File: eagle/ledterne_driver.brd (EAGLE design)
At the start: 25.9 x 24.6 mm, 15 parts, among them IC1 MEGA8-AI

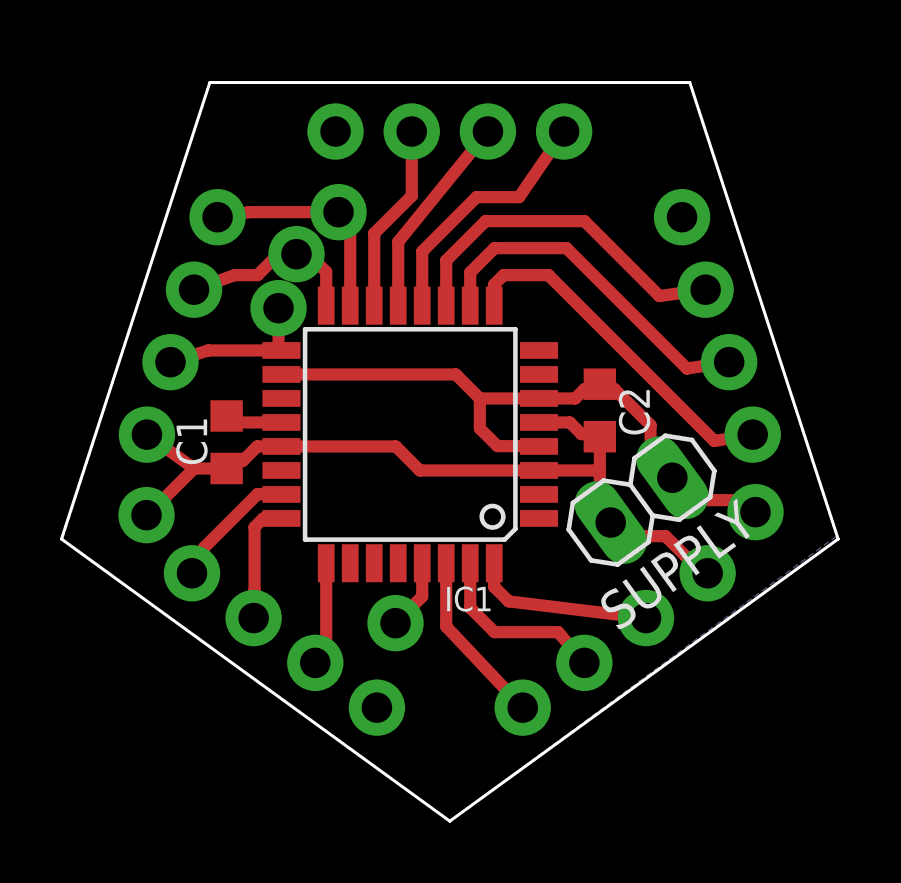
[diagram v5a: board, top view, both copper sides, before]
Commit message: Switch to a slightly larger capacitor package
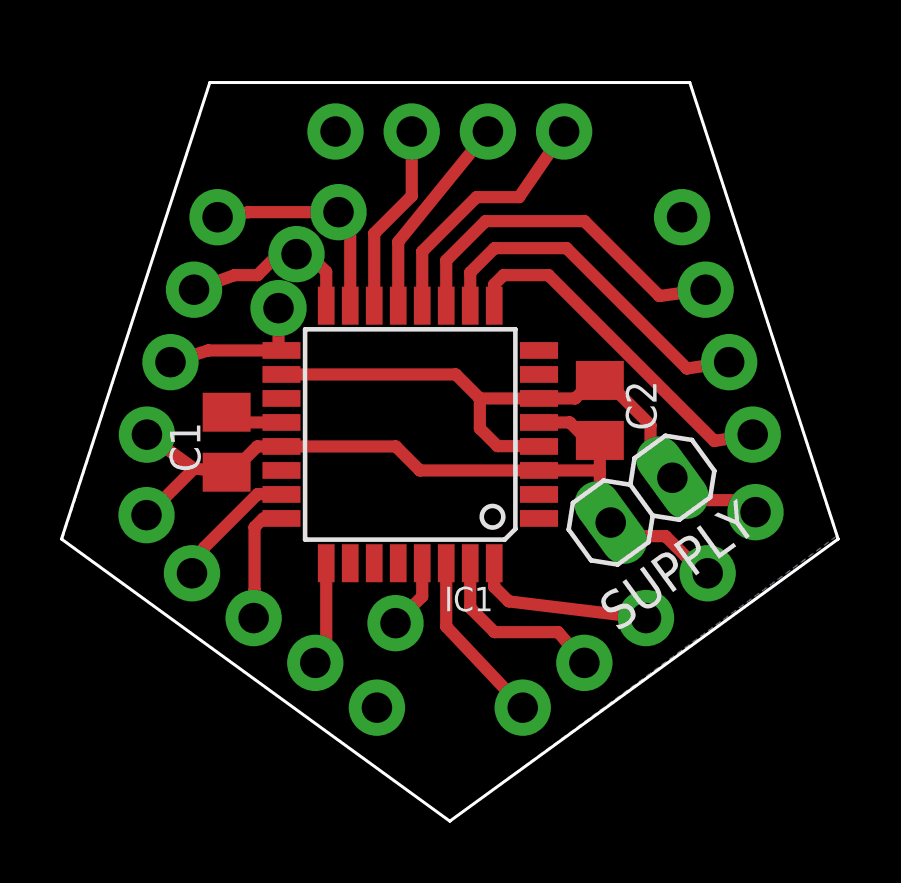
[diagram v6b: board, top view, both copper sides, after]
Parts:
- C1, C2: device rcl:C0603K -> rcl:C0805K
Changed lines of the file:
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@@
 <attribute name="MPN" value="ATMEGA8-16AU" x="15.19" y="15.79" size="1.778" layer="27" rot="R180" display="off"/>
 </element>
-<element name="C1" library="rcl" package="C0603K" value="100n" x="9.07" y="15.53" rot="R90"/>
-<element name="C2" library="rcl" package="C0603K" value="100n" x="21.51" y="16.59" rot="R270"/>
+<element name="C1" library="rcl" package="C0805K" value="100n" x="9.07" y="15.53" rot="R90"/>
+<element name="C2" library="rcl" package="C0805K" value="100n" x="21.51" y="16.59" rot="R270"/>
 <element name="JP1" library="pinhead_round_pads" package="1X04/90" value="" x="16.51" y="29.69815625" rot="MR0"/>
 <element name="JP2" library="pinhead_round_pads" package="1X04/90" value="" x="29.05268125" y="20.5853625" rot="MR72"/>
@@
 <wire x1="15.51" y1="14.59" x2="14.71" y2="15.39" width="0.4064" layer="1"/>
 <wire x1="14.71" y1="15.39" x2="10.8974" y2="15.39" width="0.4064" layer="1"/>
-<wire x1="21.51" y1="15.715" x2="21.51" y2="14.5" width="0.4064" layer="1"/>
+<wire x1="21.51" y1="15.59" x2="21.51" y2="14.5" width="0.4064" layer="1"/>
 <wire x1="21.51" y1="14.5" x2="21.51" y2="13.216059375" width="0.4064" layer="1"/>
 <wire x1="21.51" y1="13.216059375" x2="21.872546875" y2="12.8535125" width="0.4064" layer="1"/>
 <wire x1="19.4826" y1="14.59" x2="21.42" y2="14.59" width="0.4064" layer="1"/>
 <wire x1="21.42" y1="14.59" x2="21.51" y2="14.5" width="0.4064" layer="1"/>
-<wire x1="9.07" y1="14.655" x2="7.984796875" y2="14.655" width="0.4064" layer="1"/>
+<wire x1="9.07" y1="14.53" x2="7.984796875" y2="14.655" width="0.4064" layer="1"/>
 <wire x1="7.984796875" y1="14.655" x2="6.413490625" y2="15.78448125" width="0.4064" layer="1"/>
 <wire x1="19.4826" y1="16.19" x2="20.51" y2="16.19" width="0.4064" layer="1"/>
 <wire x1="20.51" y1="16.19" x2="20.9" y2="15.8" width="0.4064" layer="1"/>
 <wire x1="20.9" y1="15.8" x2="21.425" y2="15.8" width="0.4064" layer="1"/>
-<wire x1="21.425" y1="15.8" x2="21.51" y2="15.715" width="0.4064" layer="1"/>
+<wire x1="21.425" y1="15.8" x2="21.51" y2="15.59" width="0.4064" layer="1"/>
 <wire x1="21.872546875" y1="12.8535125" x2="22.326059375" y2="12.4" width="0.4064" layer="1"/>
 <wire x1="22.326059375" y1="12.4" x2="23.7" y2="12.4" width="0.4064" layer="1"/>
@@
 <wire x1="10.09" y1="15.39" x2="9.6" y2="14.9" width="0.4064" layer="1"/>
 <wire x1="9.6" y1="14.9" x2="9.315" y2="14.9" width="0.4064" layer="1"/>
-<wire x1="9.315" y1="14.9" x2="9.07" y2="14.655" width="0.4064" layer="1"/>
+<wire x1="9.315" y1="14.9" x2="9.07" y2="14.53" width="0.4064" layer="1"/>
 <wire x1="6.4" y1="13.1" x2="6.429796875" y2="13.1" width="0.4064" layer="1"/>
 <wire x1="6.429796875" y1="13.1" x2="7.984796875" y2="14.655" width="0.4064" layer="1"/>
@@
 <wire x1="20.69" y1="16.99" x2="21" y2="17.3" width="0.4064" layer="1"/>
 <wire x1="21" y1="17.3" x2="21.345" y2="17.3" width="0.4064" layer="1"/>
-<wire x1="21.345" y1="17.3" x2="21.51" y2="17.465" width="0.4064" layer="1"/>
+<wire x1="21.345" y1="17.3" x2="21.51" y2="17.59" width="0.4064" layer="1"/>
 <wire x1="21.345" y1="17.3" x2="22" y2="17.3" width="0.4064" layer="1"/>
 <wire x1="22" y1="17.3" x2="23.2" y2="16.1" width="0.4064" layer="1"/>
@@
 <contactref element="IC1" pad="20"/>
 <wire x1="10.8974" y1="16.19" x2="9.385" y2="16.19" width="0.4064" layer="1"/>
-<wire x1="9.385" y1="16.19" x2="9.07" y2="16.405" width="0.4064" layer="1"/>
+<wire x1="9.385" y1="16.19" x2="9.07" y2="16.53" width="0.4064" layer="1"/>
 </signal>
 <signal name="N$3">

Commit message: Finally fix the routing again
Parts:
- moved SCK 1.70 mm to (9.60, 18.8)
- moved MOSI 1.25 mm to (13.9, 23.8)
- moved GND 0.92 mm to (5.50, 12.9)
- moved MISO 0.86 mm to (10.7, 21.3)
- moved VCC 0.85 mm to (27.5, 12.9)
- moved SUPPLY 0.73 mm to (23.6, 13.4)
- moved IC1 0.73 mm to (15.9, 15.6)
- moved C2 0.73 mm to (22.2, 16.4)
- moved RESET 0.64 mm to (15.1, 9.00)
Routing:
- net MOSI: track 7.32 -> 9.39 mm
- net N$1: track 1.98 -> 3.21 mm
- net N$7: track 11.8 -> 10.9 mm
- net N$6: track 11.7 -> 10.9 mm
- net N$10: track 6.10 -> 5.27 mm
- net N$12: track 4.27 -> 5.08 mm
- net N$5: track 8.44 -> 7.67 mm
- net GND: track 27.6 -> 28.3 mm
- net N$11: track 6.08 -> 5.50 mm
- net N$3: track 6.32 -> 6.86 mm
- net N$8: track 11.8 -> 11.2 mm

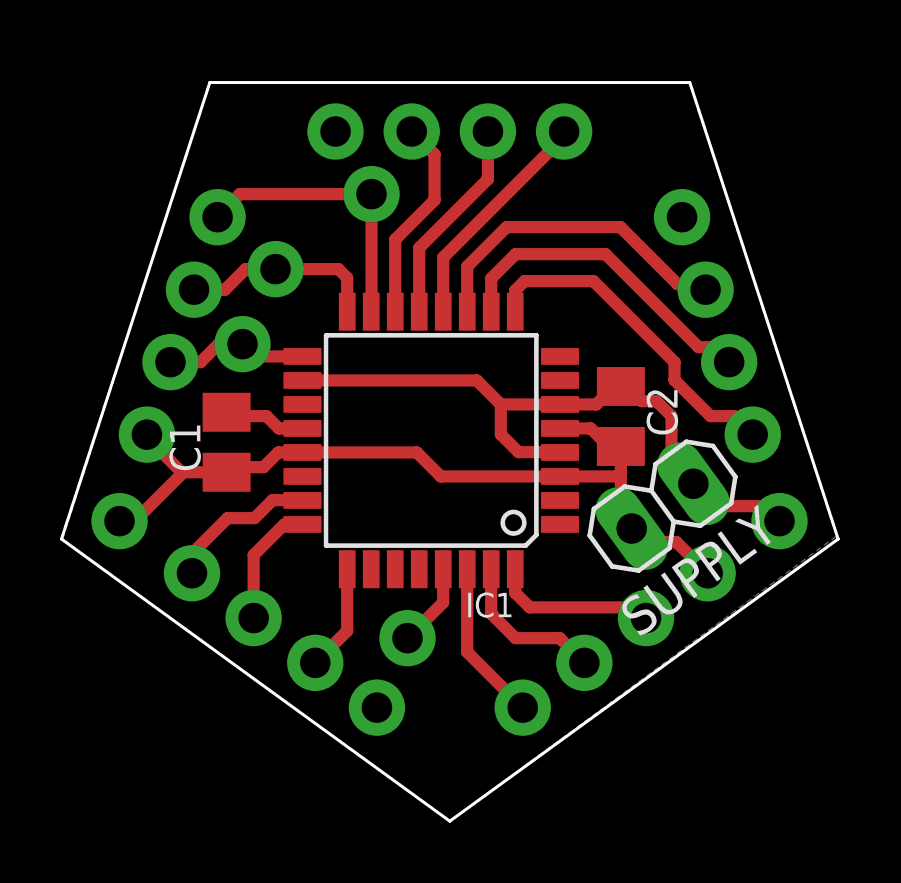
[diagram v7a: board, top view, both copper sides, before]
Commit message: Add drills for attaching mounts to the driver board
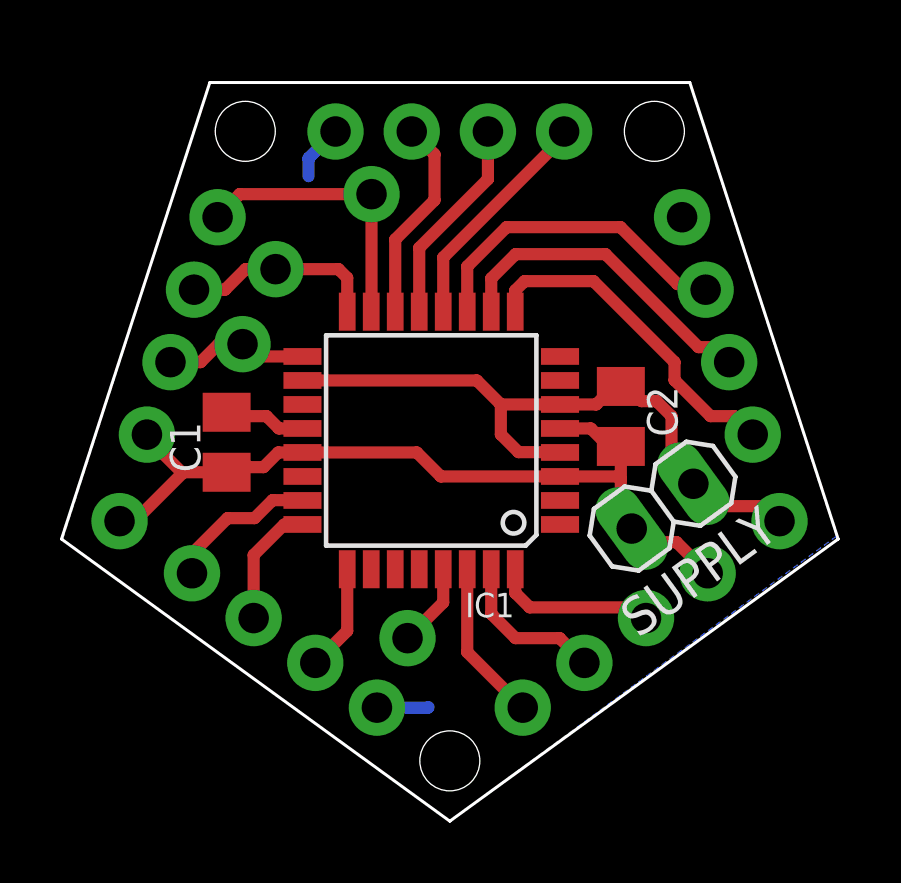
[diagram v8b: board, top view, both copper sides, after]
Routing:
- net GND: track 28.3 -> 31.9 mm
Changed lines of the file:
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@@
 <layer number="43" name="vRestrict" color="2" fill="10" visible="yes" active="yes"/>
 <layer number="44" name="Drills" color="7" fill="1" visible="no" active="yes"/>
-<layer number="45" name="Holes" color="7" fill="1" visible="no" active="yes"/>
+<layer number="45" name="Holes" color="7" fill="1" visible="yes" active="yes"/>
 <layer number="46" name="Milling" color="3" fill="1" visible="no" active="yes"/>
 <layer number="47" name="Measures" color="7" fill="1" visible="yes" active="yes"/>
@@
 <wire x1="24.51" y1="33.02" x2="24.51" y2="31.75" width="0.1" layer="47"/>
 <wire x1="24.51" y1="31.75" x2="24.51" y2="30.48" width="0.1" layer="47"/>
+<hole x="23.3283" y="25.8946" drill="2"/>
+<hole x="16.51" y="4.91" drill="2"/>
+<hole x="9.6917" y="25.8946" drill="2"/>
 </plain>
 <attributes>
@@
 <wire x1="23.026059375" y1="12.2" x2="24.067071875" y2="12.2" width="0.4064" layer="1"/>
 <wire x1="24.067071875" y1="12.2" x2="25.104696875" y2="11.162375" width="0.4064" layer="1"/>
+<wire x1="14.080015625" y1="6.68345" x2="15.78345" y2="6.68345" width="0.4064" layer="16"/>
+<wire x1="15.78345" y1="6.68345" x2="15.8" y2="6.7" width="0.4064" layer="16"/>
+<wire x1="12.7" y1="25.88815625" x2="12.68815625" y2="25.88815625" width="0.4064" layer="16"/>
+<wire x1="12.68815625" y1="25.88815625" x2="11.8" y2="25" width="0.4064" layer="16"/>
+<wire x1="11.8" y1="25" x2="11.8" y2="24.4" width="0.4064" layer="16"/>
 </signal>
 <signal name="VCC">
